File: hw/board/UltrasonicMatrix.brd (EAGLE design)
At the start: 140 x 150 mm, 180 parts, among them IC1 7812L, U1 TC4427EOA, U10 TC4427EOA, U11 TC4427EOA, U12 TC4427EOA, U13 TC4427EOA, U14 TC4427EOA, U15 TC4427EOA, U16 TC4427EOA, U17 TC4427EOA, U18 TC4427EOA, U19 TC4427EOA, U2 TC4427EOA, U20 TC4427EOA, U21 TC4427EOA, U22 TC4427EOA, U23 TC4427EOA, U24 TC4427EOA, U25 TC4427EOA, U26 TC4427EOA, U27 TC4427EOA, U28 TC4427EOA, U29 TC4427EOA, U3 TC4427EOA, U30 TC4427EOA, U31 TC4427EOA, U32 TC4427EOA, U4 TC4427EOA, U5 TC4427EOA, U6 TC4427EOA, U7 TC4427EOA, U8 TC4427EOA, U9 TC4427EOA

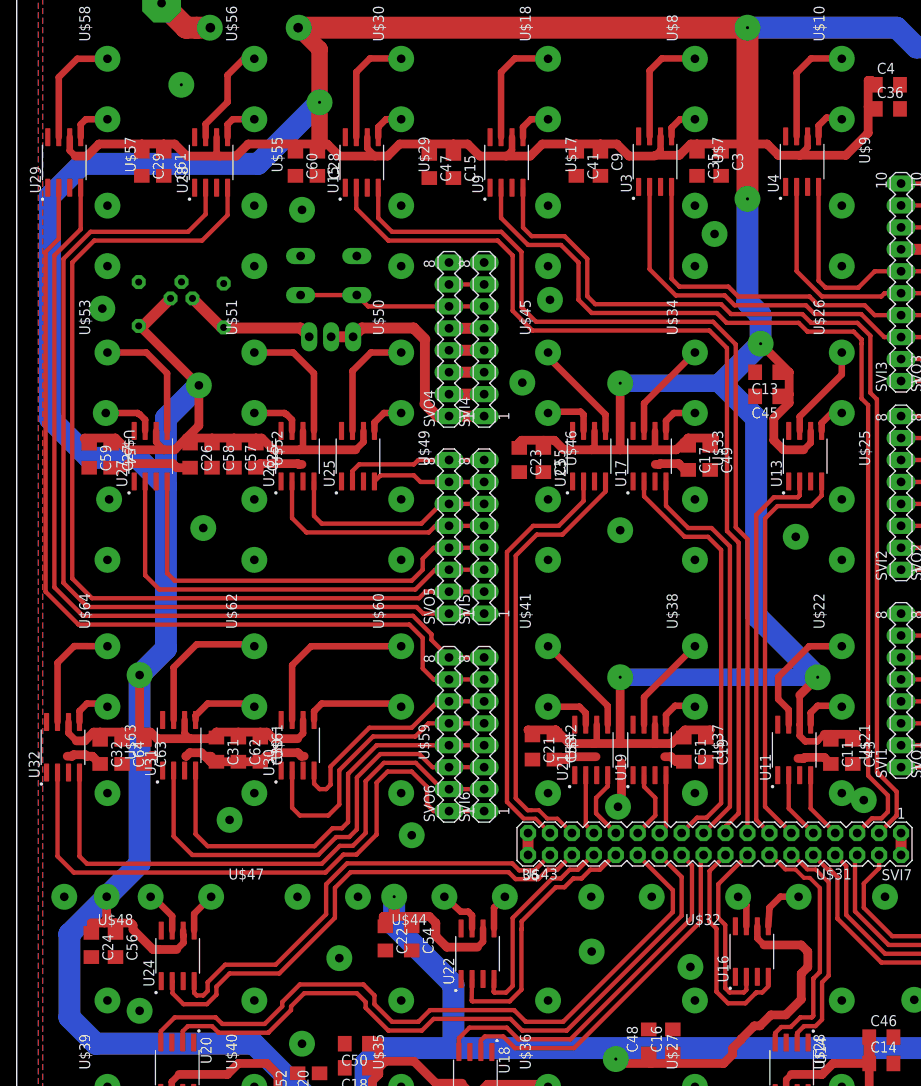
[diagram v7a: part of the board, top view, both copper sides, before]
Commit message: Board design enhancments
* New alignment marks
* Increased thermal isolation to 20mil
* Upgraded PCBtest to new design rules with 20mil clearance and increased text size to test the same object sizes of the main board
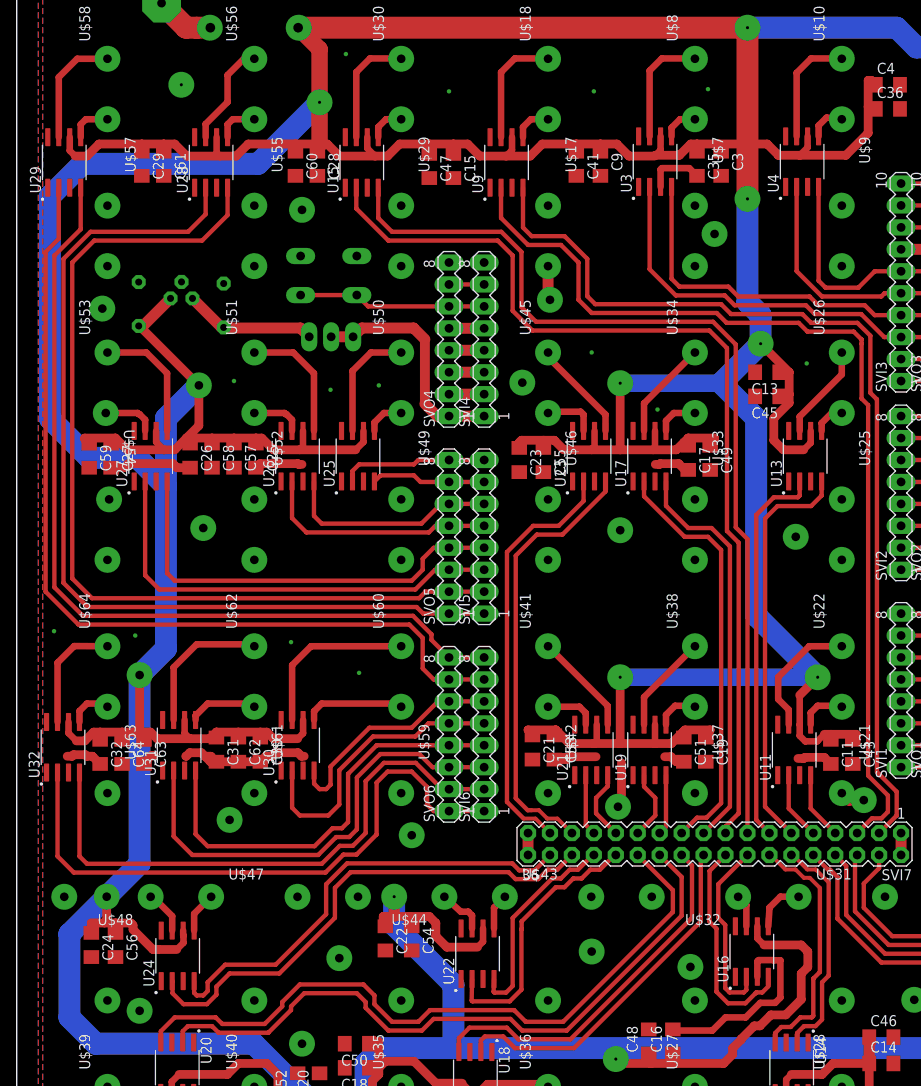
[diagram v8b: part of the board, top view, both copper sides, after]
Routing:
- net GND: track 75.2 -> 111.6 mm, vias 22 -> 36
